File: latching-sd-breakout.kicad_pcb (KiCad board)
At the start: 2 copper layers, 26.6 x 24 mm, 7 parts, among them X1 microSD

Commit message: pass drc
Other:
- board text added: "Meowvionics Sense :3"
- board text removed: "Rachelle Wang"
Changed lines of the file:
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@@
 		(tags "472192001 ")
 		(property "Reference" "X1"
-			(at 0 2.098299 180)
+			(at -0.185001 -0.091701 0)
 			(unlocked yes)
 			(layer "F.SilkS")
@@
 		)
 		(fp_text user "${REFERENCE}"
-			(at 0 2.098299 180)
+			(at -0.185001 2.108299 0)
 			(unlocked yes)
 			(layer "F.Fab")
@@
 		(tags "resistor array")
 		(property "Reference" "R2"
-			(at 0 -2.8 0)
+			(at -0.01 -2.99 0)
 			(layer "F.SilkS")
 			(effects
@@
 		)
 		(property "Value" "47K"
-			(at 0 2.8 0)
+			(at -0.41 3.41 0)
 			(layer "F.Fab")
 			(effects
@@
 		(tags "capacitor")
 		(property "Reference" "C2"
-			(at 0 -1.43 90)
+			(at 0.51 -1.49 90)
 			(layer "F.SilkS")
 			(effects
@@
 		)
 		(property "Value" "0.1uF"
-			(at 0 1.43 90)
+			(at 0 1.41 90)
 			(layer "F.Fab")
 			(effects
@@
 		)
 		(property "Value" "HEADER-1X970MIL"
-			(at 0 -2.5 0)
+			(at 0 2.31 0)
 			(layer "F.Fab")
 			(effects
@@
 		(tags "resistor array")
 		(property "Reference" "R1"
-			(at 0 -2.8 0)
+			(at -1.59 -2.61 0)
 			(layer "F.SilkS")
 			(effects
@@
 			(at 0 0 0)
 			(layer "F.SilkS")
+			(hide yes)
 			(effects
 				(font
@@
 		(layer "Edge.Cuts")
 	)
-	(gr_text "Rachelle Wang"
-		(at 131.736499 88.929599 0)
+	(gr_text "Meowvionics\nSense :3"
+		(at 131.4 87.9 0)
 		(layer "B.SilkS")
 		(effects
 			(font
 				(size 1 1)
-				(thickness 0.1)
-			)
-			(justify left bottom mirror)
+				(thickness 0.125)
+			)
+			(justify left mirror)
 		)
 	)

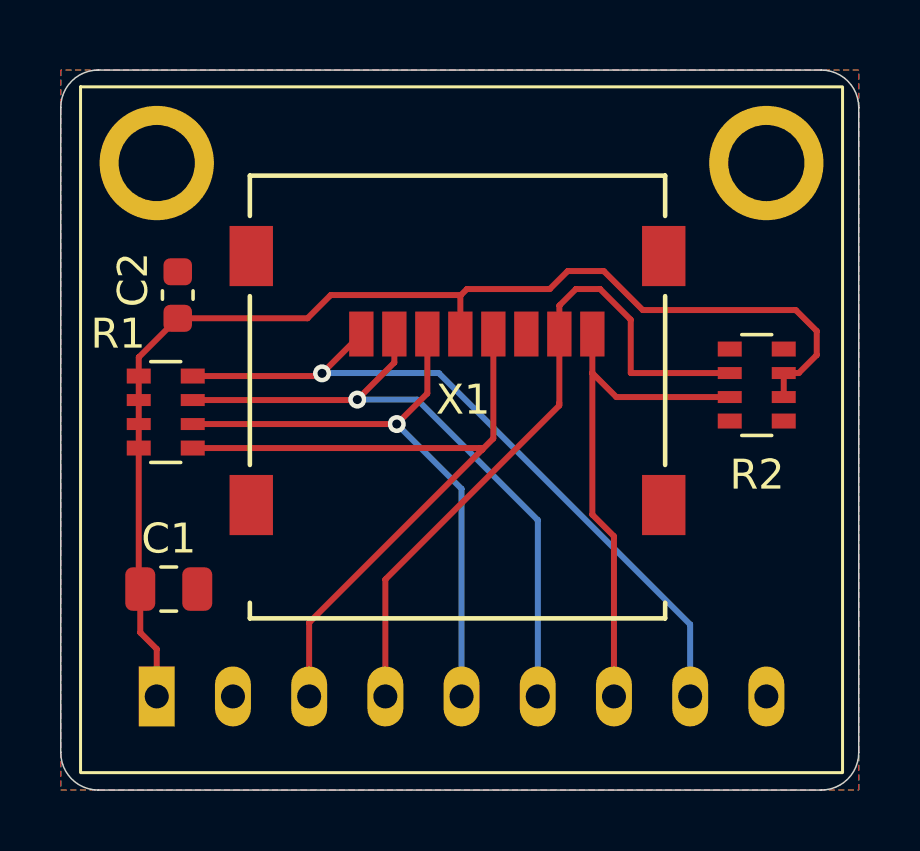
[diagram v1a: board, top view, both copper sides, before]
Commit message: fix routing angles
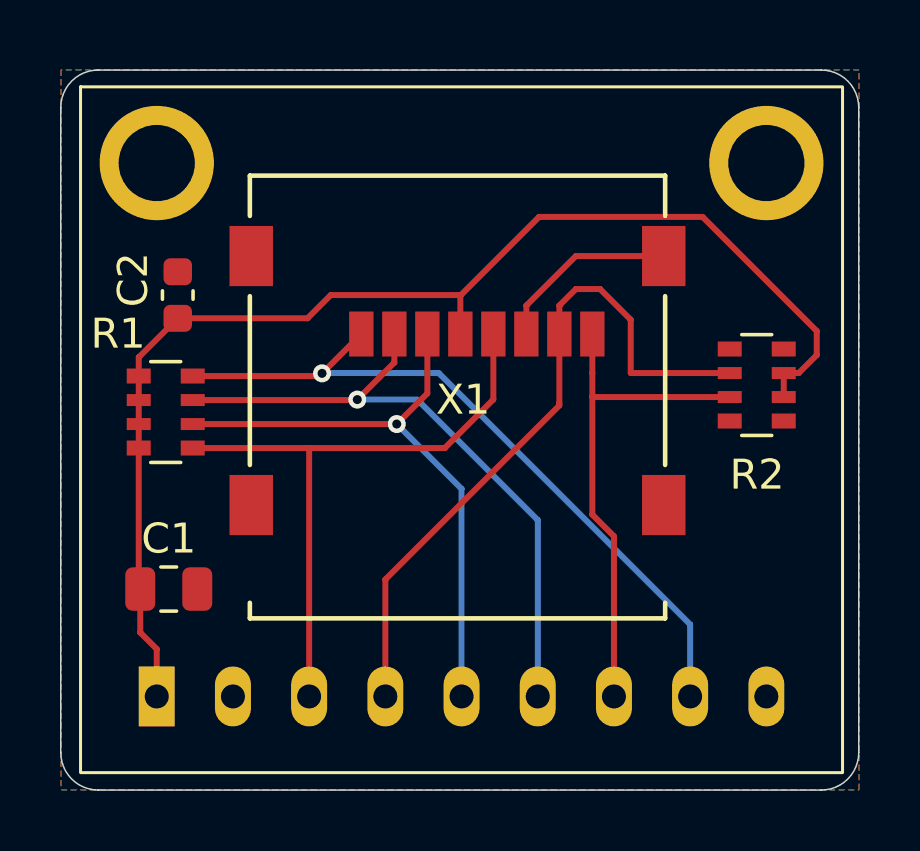
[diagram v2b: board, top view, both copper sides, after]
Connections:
- X1 pad 6: (no net) -> GND
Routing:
- net GND: track 0.00 -> 6.21 mm
- net /SCLK: track 24.3 -> 21.2 mm
- net 3.3V: track 40.4 -> 41.9 mm
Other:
- board text added: "UCSC Rocket Team Meowvionics :3"
- board text removed: "Meowvionics Sense :3"

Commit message: changed resistor arrays
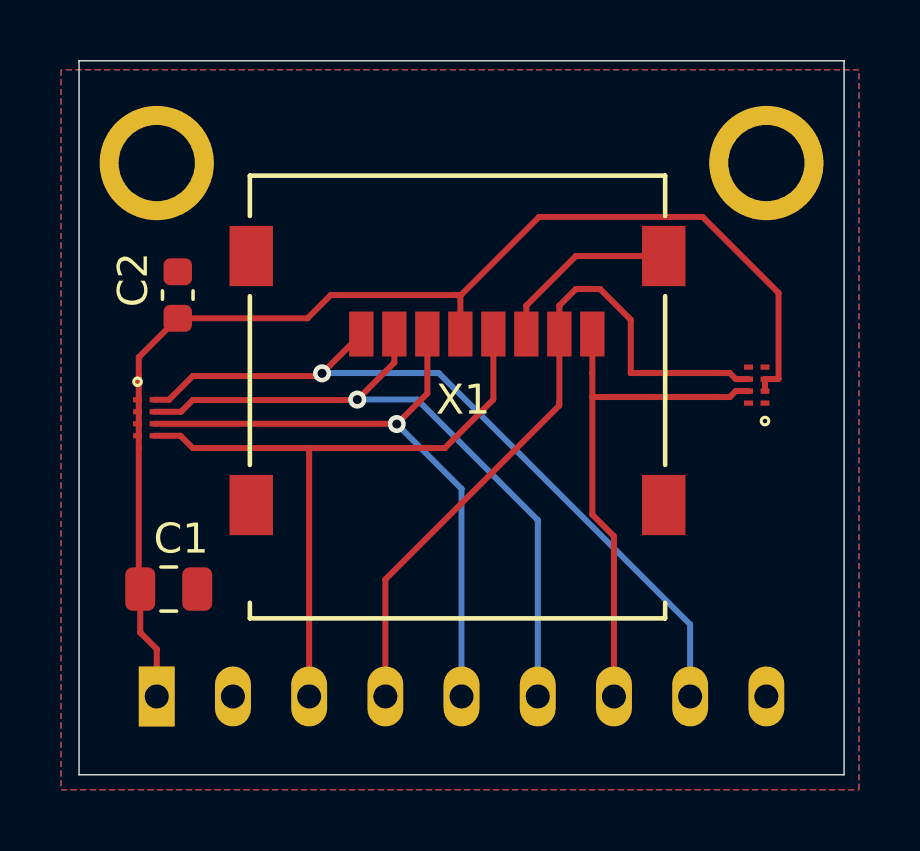
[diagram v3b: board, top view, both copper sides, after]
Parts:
- R1, R2: footprint Resistor_SMD:R_Array_Convex_4x0603 -> Resistor_SMD:R_Array_Convex_4x0502
- moved R1 0.69 mm to (114.4, 97.0), turned to -90 degrees
- turned R2 to 90 degrees
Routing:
- net /DAT2: track 24.3 -> 26.0 mm
- net /SCLK: track 21.2 -> 22.6 mm
- net /CS: track 21.7 -> 23.2 mm
- net /DI: track 20.2 -> 21.5 mm
- net 3.3V: track 41.9 -> 40.9 mm
- net /DAT1: track 17.0 -> 17.7 mm
- net /DO: track 23.5 -> 24.2 mm
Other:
- board size 26.6 x 24 mm -> 25.5 x 23.8 mm
